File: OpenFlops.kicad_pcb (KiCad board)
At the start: 2 copper layers, 112 x 59 mm, 66 parts, among them J7 DISPLAY_PORT, P1 FLOPPY_CONN, P2 POWER_INPUT, P3 USB_A_FEMALE, P4 PROG_PORT, P5 JUMPERS, Q1 MOS_N_GSD, Q2 MOS_N_GSD, Q3 MOS_N_GSD, Q4 MOS_N_GSD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

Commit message: Improve power distribution
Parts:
- moved C6 6.52 mm to (160.5, 69.7), turned to 90 degrees
- moved C8 2.99 mm to (163.9, 87.2)
- moved C16 2.64 mm to (177.3, 85.7), turned to 90 degrees
- moved C7 1.73 mm to (181.1, 73.5), turned to 90 degrees
- moved J7 1.27 mm to (144.3, 96.3)
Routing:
- net +3V3: track 247.4 -> 276.3 mm, vias 7 -> 8
- net /disp_dio: track 77.1 -> 81.1 mm
- net /boot0: track 110.0 -> 113.0 mm
- net /~selx: track 126.4 -> 124.5 mm
- net /dir: track 86.3 -> 87.5 mm
- net /spi_cs: track 11.5 -> 10.4 mm
- net /jb: track 102.6 -> 103.2 mm
- net /~trk0_3v3: track 47.2 -> 47.8 mm
- net /j7_pin1: track 44.2 -> 44.7 mm
- net /j7_pin2: track 47.9 -> 48.4 mm
- net /~dskchg_3v3: track 38.7 -> 38.2 mm

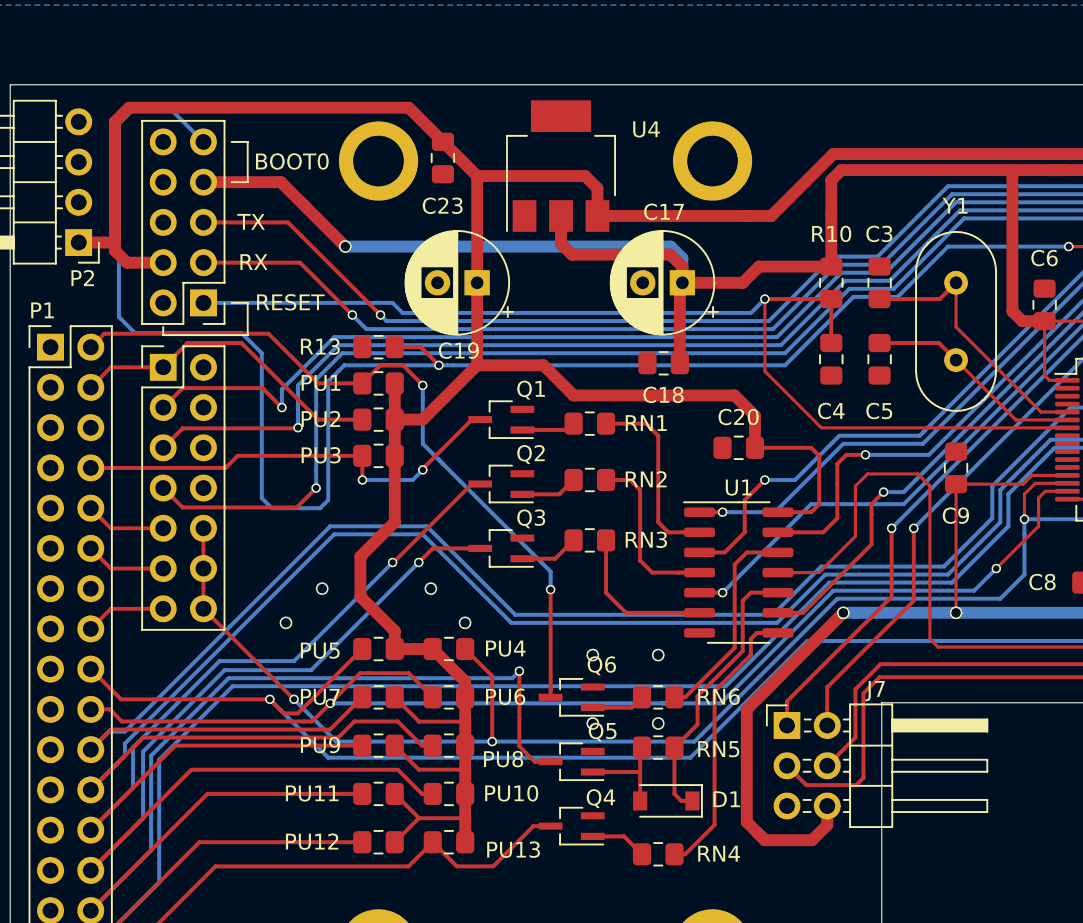
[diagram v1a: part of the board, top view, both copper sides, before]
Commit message: Put power connectors on spare P4 pins
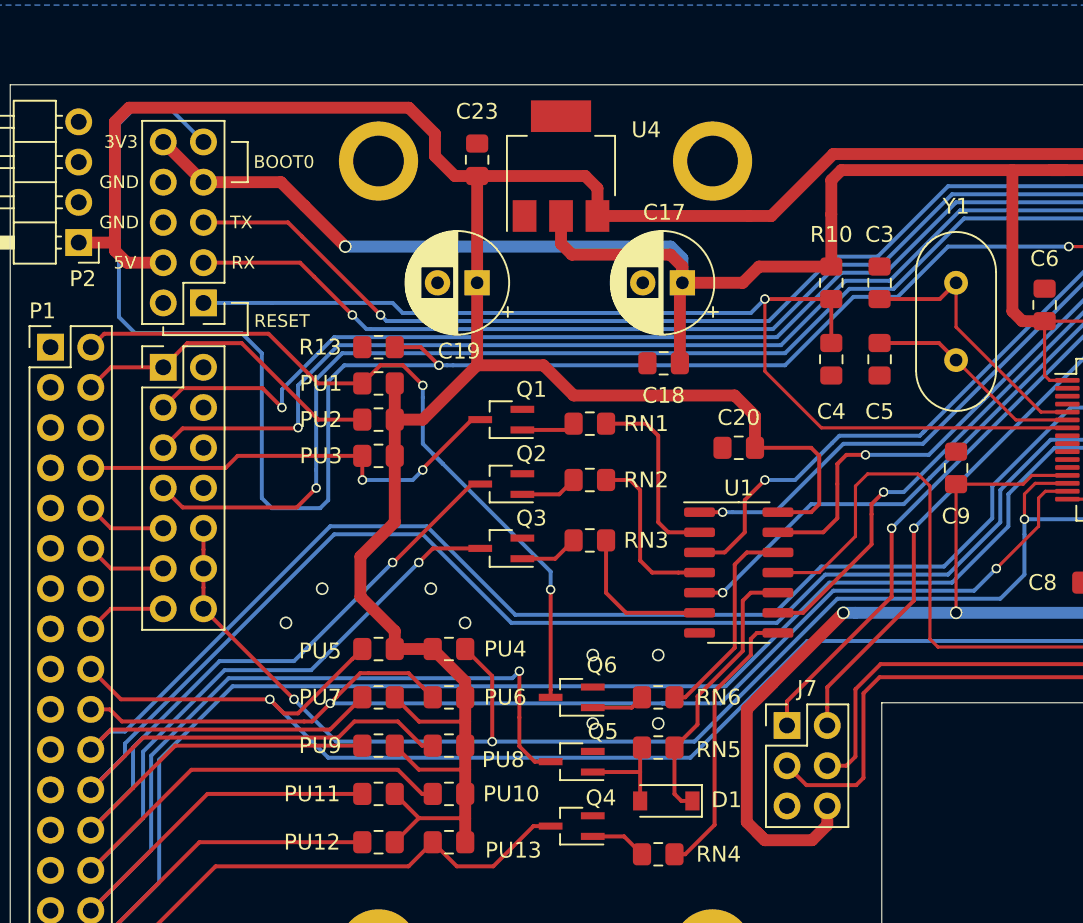
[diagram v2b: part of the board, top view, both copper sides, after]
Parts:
- J7: footprint Connector_PinHeader_2.54mm:PinHeader_2x03_P2.54mm_Horizontal -> Connector_PinHeader_2.54mm:PinHeader_2x03_P2.54mm_Vertical
- moved C23 2.16 mm to (124.7, 60.6), turned to 90 degrees
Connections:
- P4 pad 10: Net-(P4-Pad10) -> +3V3
- P4 pad 6: /swclk -> GND
- P4 pad 8: Net-(P4-Pad8) -> GND
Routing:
- net +3V3: track 276.3 -> 279.9 mm
- net +5V: track 252.8 -> 253.6 mm
- net /disp_dio: track 81.1 -> 81.8 mm
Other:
- board text added: "3V3"
- board text added: "5V"
- board text added: "GND"

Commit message: Fix track width
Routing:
- net /disp_dio: track 81.8 -> 79.7 mm
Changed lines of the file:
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@@
     (thickness 1.6)
     (drawings 24)
-    (tracks 766)
+    (tracks 764)
     (zones 0)
     (modules 66)
@@
   (segment (start 195.199 69.024499) (end 195.135501 69.024499) (width 0.25) (layer B.Cu) (net 12))
   (segment (start 169.89 83.907) (end 169.89 90.388) (width 0.2) (layer F.Cu) (net 12))
-  (segment (start 167.8855 92.3925) (end 169.8265 90.4515) (width 0.25) (layer F.Cu) (net 12))
-  (segment (start 169.8265 90.4515) (end 168.33 91.948) (width 0.2) (layer F.Cu) (net 12))
-  (segment (start 169.89 90.388) (end 169.8265 90.4515) (width 0.2) (layer F.Cu) (net 12))
   (via (at 167.8855 92.3925) (size 0.6) (drill 0.4) (layers F.Cu B.Cu) (net 12))
   (segment (start 168.965 93.472) (end 170.688 93.472) (width 0.25) (layer B.Cu) (net 12))
@@
   (segment (start 148.59 98.230081) (end 148.59 93.98) (width 0.25) (layer F.Cu) (net 12))
   (segment (start 146.812 98.806) (end 148.014081 98.806) (width 0.25) (layer F.Cu) (net 12))
+  (segment (start 169.89 90.388) (end 167.8855 92.3925) (width 0.2) (layer F.Cu) (net 12))
   (via (at 125.6665 97.282) (size 0.6) (drill 0.4) (layers F.Cu B.Cu) (net 13))
   (via (at 113.157 94.615) (size 0.6) (drill 0.4) (layers F.Cu B.Cu) (net 13))
@@
     (connect_pads (clearance 0.254))
     (min_thickness 0.0254)
-    (fill yes (arc_segments 32) (thermal_gap 0.508) (thermal_bridge_width 0.508))
+    (fill (arc_segments 32) (thermal_gap 0.508) (thermal_bridge_width 0.508))
     (polygon
       (pts
@@
     (connect_pads (clearance 0.254))
     (min_thickness 0.0254)
-    (fill yes (arc_segments 32) (thermal_gap 0.508) (thermal_bridge_width 0.508))
+    (fill (arc_segments 32) (thermal_gap 0.508) (thermal_bridge_width 0.508))
     (polygon
       (pts

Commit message: Update PCB
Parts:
- removed C16: 100n, Capacitor_SMD:C_0805_2012Metric_Pad1.15x1.40mm_HandSolder
- removed J7: DISPLAY_PORT, Connector_PinHeader_2.54mm:PinHeader_2x03_P2.54mm_Vertical
- removed L35: LED_RED, LED_THT:LED_D3.0mm-3
- removed U8: W25Q32JVSS (?), Package_SO:SOIC-8_5.23x5.23mm_P1.27mm
- added D2: 1N5819 (?), Diode_SMD:D_SOD-123, F.Cu at (131.0, 106.7)
- added LD2: LED_RED, LED_THT:LED_D3.0mm, F.Cu at (195.2, 64.0)
- added P6: ENCODER_PORT, Connector_PinHeader_2.54mm:PinHeader_1x05_P2.54mm_Vertical, F.Cu at (162.6, 60.3)
- added P7: DISPLAY_PORT, Connector_PinHeader_2.54mm:PinHeader_1x04_P2.54mm_Vertical, F.Cu at (145.9, 96.6)
- added PU14: 1k, Resistor_SMD:R_0805_2012Metric_Pad1.15x1.40mm_HandSolder, F.Cu at (118.5, 83.8)
- added PU15: 1k, Resistor_SMD:R_0805_2012Metric_Pad1.15x1.40mm_HandSolder, F.Cu at (118.5, 81.5)
- added Q7: MMBT3904, Package_TO_SOT_SMD:SOT-23_Handsoldering, F.Cu at (130.7, 102.8)
- added R3: 3.3K, Resistor_SMD:R_0805_2012Metric_Pad1.15x1.40mm_HandSolder, F.Cu at (145.9, 108.5)
- added R4: 3.3K, Resistor_SMD:R_0805_2012Metric_Pad1.15x1.40mm_HandSolder, F.Cu at (148.5, 108.5)
- added R5: 1K, Resistor_SMD:R_0805_2012Metric_Pad1.15x1.40mm_HandSolder, F.Cu at (136.3, 103.6)
- added R6: 100, Resistor_SMD:R_0805_2012Metric_Pad1.15x1.40mm_HandSolder, F.Cu at (122.9, 106.7)
- added SPK1: Speaker, OpenFlops:Buzzer, F.Cu at (125.5, 114.0)
- moved Q4 3.88 mm to (130.7, 98.7)
- moved RN4 3.81 mm to (136.1, 100.6)
- moved D1 3.49 mm to (136.8, 97.5)
- moved Q5 3.46 mm to (130.7, 95.1)
- moved RN5 3.17 mm to (136.1, 94.5)
- moved Q6 3.05 mm to (130.7, 91.4)
- moved RN6 3.05 mm to (136.1, 91.4)
- moved U1 1.40 mm to (141.2, 85.2)
- renumbered L4 to LD1
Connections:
- P1 pad 14: /~sel2 -> (no net)
- P1 pad 6: /~sel3 -> (no net)
- P2 pad 4: Net-(P2-Pad4) -> (no net)
- P5 pad 3: /ja -> /jc
- P5 pad 5: /jc -> /~sel0
- P5 pad 6: GND -> /~sely
- P5 pad 7: /jb -> /~sel1
- P5 pad 8: GND -> /~sely
- U3 pad 10: Net-(U3-Pad10) -> (no net)
- U3 pad 11: Net-(U3-Pad11) -> (no net)
- U3 pad 17: Net-(U3-Pad17) -> /~sely
- U3 pad 2: Net-(U3-Pad2) -> GND
- U3 pad 20: Net-(U3-Pad20) -> (no net)
- U3 pad 21: Net-(U3-Pad21) -> (no net)
- U3 pad 22: Net-(U3-Pad22) -> (no net)
- U3 pad 24: Net-(U3-Pad24) -> (no net)
- U3 pad 25: Net-(U3-Pad25) -> (no net)
- U3 pad 28: Net-(U3-Pad28) -> (no net)
- U3 pad 3: Net-(U3-Pad3) -> GND
- U3 pad 33: /spi_cs -> (no net)
- U3 pad 34: /spi_clk -> (no net)
- U3 pad 35: /spi_do -> (no net)
- U3 pad 36: /spi_di -> (no net)
- U3 pad 4: Net-(U3-Pad4) -> GND
- U3 pad 40: Net-(U3-Pad40) -> (no net)
- U3 pad 46: Net-(U3-Pad46) -> (no net)
- U3 pad 49: /swclk -> (no net)
- U3 pad 50: Net-(U3-Pad50) -> /~mtron
- U3 pad 51: /j7_pin1 -> /enc_dt
- U3 pad 52: /j7_pin2 -> /enc_clk
- U3 pad 53: Net-(U3-Pad53) -> GND
- U3 pad 54: Net-(U3-Pad54) -> (no net)
- U3 pad 8: Net-(U3-Pad8) -> (no net)
- U3 pad 9: Net-(U3-Pad9) -> (no net)
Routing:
- net /~sely: track 0.00 -> 148.2 mm, vias 0 -> 3
- net /~mtron: track 5.10 -> 97.4 mm, vias 0 -> 2
- net /ja: track 95.4 -> 28.3 mm, vias 2 -> 1
- net /jb: track 103.2 -> 42.2 mm
- net /j7_pin2: track 48.4 -> 0.00 mm, vias 2 -> 0
- net /j7_pin1: track 44.7 -> 0.00 mm, vias 2 -> 0
- net /disp_clk: track 81.1 -> 45.6 mm, vias 1 -> 0
- net /disp_dio: track 79.7 -> 47.7 mm, vias 1 -> 0
- net /spi_do: track 30.3 -> 0.00 mm
- net /spi_di: track 24.4 -> 0.00 mm
- net /spi_clk: track 20.3 -> 0.00 mm
- net /enc_clk: track 0.00 -> 18.1 mm
- net Net-(D2-Pad1): track 0.00 -> 15.8 mm
- net Net-(D2-Pad2): track 0.00 -> 13.4 mm
- net /enc_dt: track 0.00 -> 13.0 mm
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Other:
- board size 112 x 59 mm -> 112 x 59.3 mm
- board text added: "0"
- board text added: "1"
- board text added: "DRV0"
- board text added: "DRV1"
- board text added: "J5"
- board text added: "JC"
- board text added: "M0"

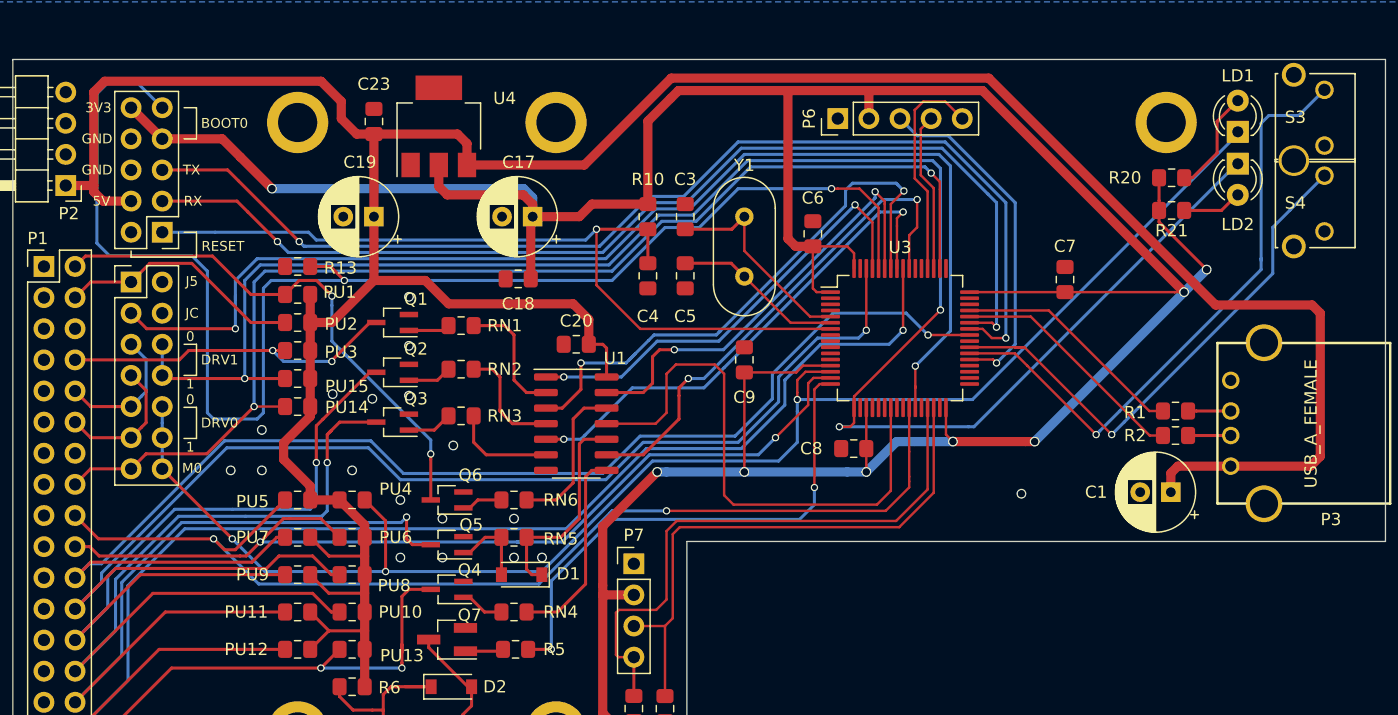
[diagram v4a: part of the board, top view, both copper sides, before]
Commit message: Improve ground plane
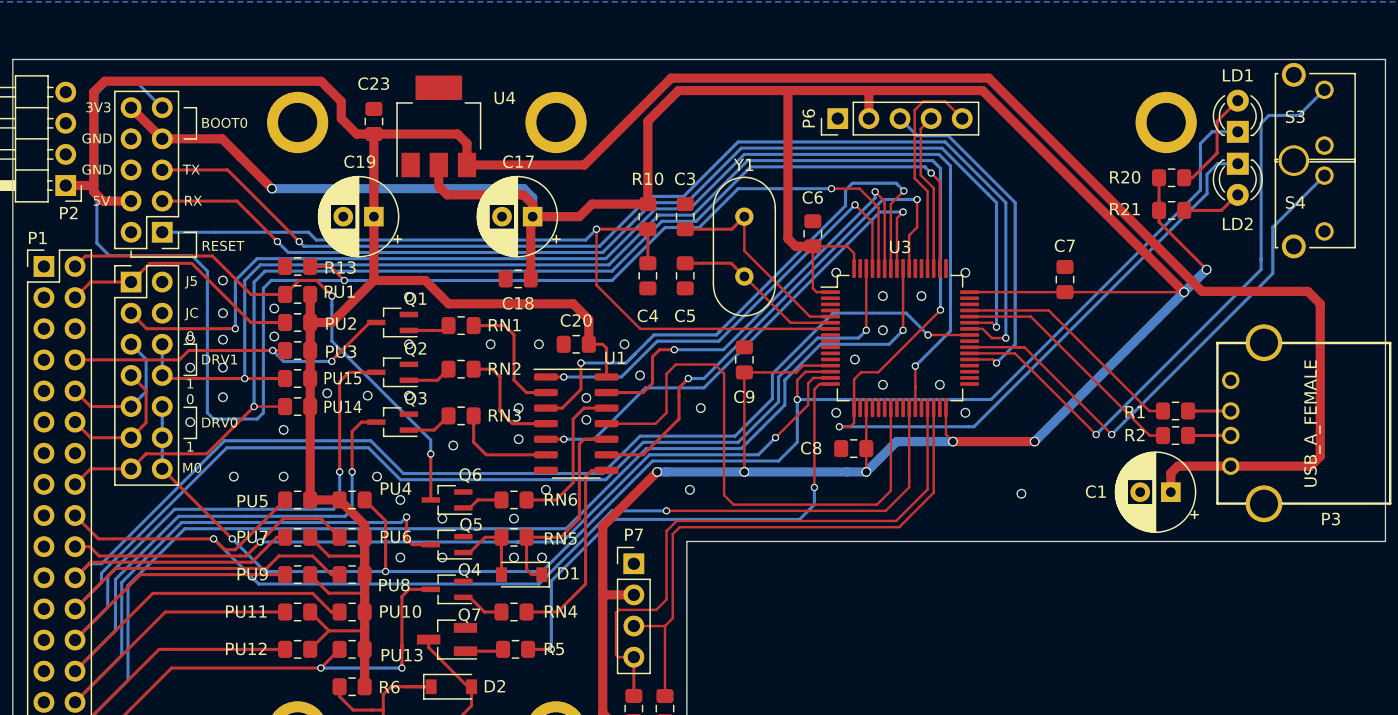
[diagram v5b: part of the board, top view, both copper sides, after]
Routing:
- net /~trk0: track 58.1 -> 60.8 mm
- net /~selx: track 124.5 -> 126.6 mm
- net /~sely: track 148.2 -> 149.9 mm
- net +5V: track 253.2 -> 251.8 mm
- net GND: vias 18 -> 49
